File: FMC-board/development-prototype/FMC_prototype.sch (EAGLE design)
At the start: 83 parts, among them J1 PJ-102AH, J2 DC_POWER_JACK-PJ-102AH, U1 TPS79301, U10 ADN4664, U11 ADN4663, U2 TPS79333, U3 ADN4663, U4 ADN4663, U5 ADN4664, U6 PDS1-S12-S5-S, U7 TPS79301, U9 ADN4664

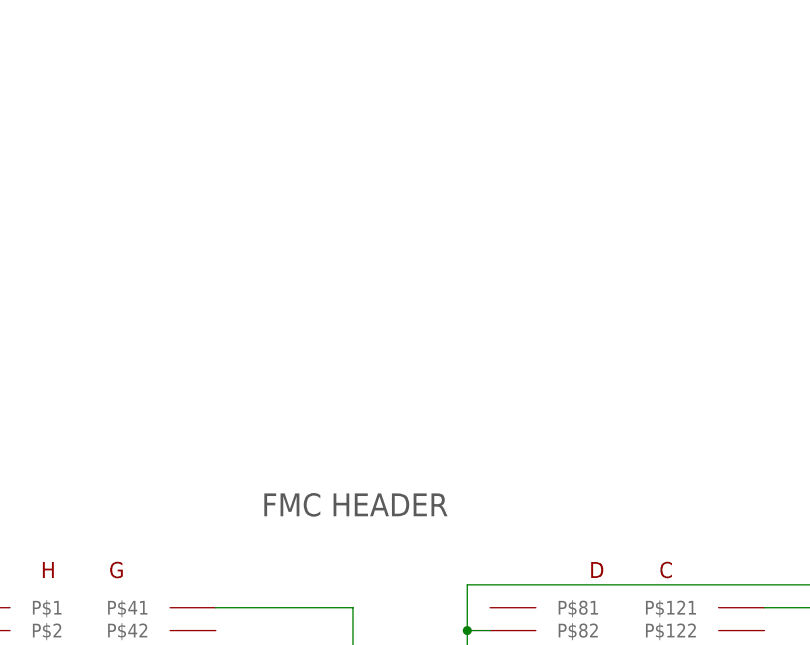
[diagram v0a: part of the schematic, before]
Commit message: Toward meeting fmc standards
- I read the VITA 57.1 standard and I think it would be worth it to make
  the board marginally compliant (even on first run) because it is not
  very dense and this really will inform the future design of the board
- Also, it will make it compatible with 100's of carrier boards with all
  sorts of FPGAs and DSPs onboard
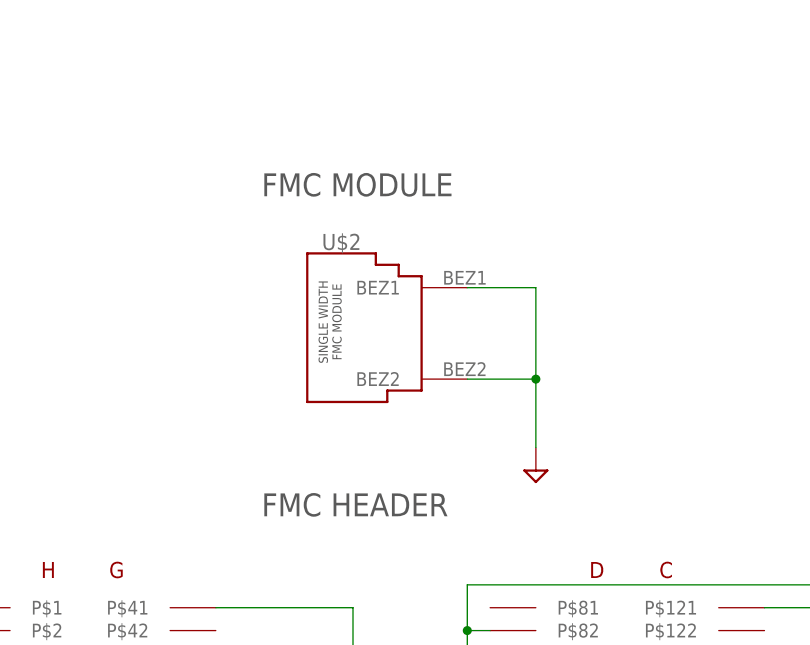
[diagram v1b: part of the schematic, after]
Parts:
- added U$2: FMC_SINGLE_WIDTH_MODULE, jonnew:FMC_SINGLE_WIDTH_MODULE
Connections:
- net GND_ISO: now also U$2.BEZ1, U$2.BEZ2
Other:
- note added: "FMC MODULE"
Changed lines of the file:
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@@
 <part name="GND15" library="supply1" deviceset="GND" device=""/>
 <part name="PWR1" library="jonnew" deviceset="+3V3" device=""/>
+<part name="U$2" library="jonnew" deviceset="FMC_SINGLE_WIDTH_MODULE" device=""/>
+<part name="PWR2" library="jonnew" deviceset="GND_ISO" device=""/>
 </parts>
 <sheets>
@@
 <text x="233.68" y="20.32" size="2.54" layer="97" rot="R90">AQ. BOARD SIDE</text>
 <text x="424.18" y="314.96" size="2.54" layer="97">FMC HEADER</text>
+<text x="424.18" y="350.52" size="2.54" layer="97">FMC MODULE</text>
 </plain>
 <instances>
@@
 <instance part="GND15" gate="1" x="434.34" y="200.66" rot="MR0"/>
 <instance part="PWR1" gate="PWR1" x="459.74" y="198.12"/>
+<instance part="U$2" gate="G$1" x="441.96" y="335.28"/>
+<instance part="PWR2" gate="G$1" x="454.66" y="322.58"/>
 </instances>
 <busses>
@@
 <junction x="91.44" y="96.52"/>
 <pinref part="GND64" gate="G$1" pin="GND_ISO"/>
+</segment>
+<segment>
+<pinref part="U$2" gate="G$1" pin="BEZ2"/>
+<wire x1="447.04" y1="330.2" x2="454.66" y2="330.2" width="0.1524" layer="91"/>
+<wire x1="454.66" y1="330.2" x2="454.66" y2="322.58" width="0.1524" layer="91"/>
+<pinref part="U$2" gate="G$1" pin="BEZ1"/>
+<wire x1="447.04" y1="340.36" x2="454.66" y2="340.36" width="0.1524" layer="91"/>
+<wire x1="454.66" y1="340.36" x2="454.66" y2="330.2" width="0.1524" layer="91"/>
+<junction x="454.66" y="330.2"/>
+<pinref part="PWR2" gate="G$1" pin="GND_ISO"/>
 </segment>
 </net>
@@
 </schematic>
 </drawing>
+<compatibility>
+<note version="6.3" minversion="6.2.2" severity="warning">
+Since Version 6.2.2 text objects can contain more than one line,
+which will not be processed correctly with this version.
+</note>
+</compatibility>
 </eagle>

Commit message: Toward VITA-57.1 compliance
- Found pad alignment issues in the SOIC16 digital isolation chips.
  Fixed that.
- Layout changes informed by VITA 57.1 and several FMC modules designed
  by CERN for data collection in high-energy physics experiments.
- Removed power jacks for now. Replaced with simple headers and reverse
  polarity protection to make up for the automatic polarity protection
  given by center positive jack (assuming the user uses the correct wall
  wart).
- High-frequency layout improvments
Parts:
- removed J1: PJ-102AH, RHD2000_eval_board:DC_POWER_JACK-PJ-102AH
- removed J2: DC_POWER_JACK-PJ-102AH, RHD2000_eval_board:DC_POWER_JACK-PJ-102AH
- removed TP1, TP2, TP3, TP4, TP5: TP5P5-25-13, testpad:TP5P5-25-13
- added C17, C20, C24, C27, C28, C29: 100n, RHD2000_eval_board:C_0603
- added C30, C31: 22uF, jonnew:C-POL_1210
- added D4: 8V, jonnew:Z-DIODE_SOD-323
- added R13: 10k, RHD2000_eval_board:R_0603
- added U$3: (no value), jonnew:JP2E_THRU-HOLE
- added U$4: SSM3J328R, jonnew:P-MOSFET_SOT23-GSD
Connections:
- removed net VDD_IN: C16.1, J2.PWR, LINK-5V.1, TP4D.TP, U7.EN, U7.IN
- new net AUX_VDD: C16.1, D4.C, LINK-5V.1, U$4.S, U7.EN, U7.IN
- new net N$6: D4.A, R13.2, U$4.G
- new net N$7: U$3.1, U$4.D
- net +3V3: now also C17.2, C20.2, C24.2, C27.2; no longer TP4B.TP, TP4C.TP
- net +3V3_ISO: no longer TP3C.TP
- net +3V6: no longer TP4A.TP
- net +3V6_ISO: no longer TP3B.TP
- net +5V0_EXT: no longer J1.PWR
- net +5V0_ISO: no longer TP3D.TP
- net 12V_FPGA: now also C28.2, C29.2, C30.+, C31.+
- net B_CS+: no longer TP5A.TP
- net B_MISO1+: no longer TP5D.TP
- net B_MISO2+: no longer TP5E.TP
- net B_MOSI+: no longer TP5C.TP
- net B_SCLK+: no longer TP5B.TP
- net GND: now also C17.1, C20.1, C24.1, C27.1, C28.1, C29.1, C30.-, C31.-, R13.1, U$3.2; no longer J2.GND1, J2.GND2, TP2E.TP, TP4E.TP
- net GND_ISO: no longer J1.GND1, J1.GND2, TP1A.TP, TP3A.TP, TP3E.TP
- net MISO1+: no longer TP2B.TP
- net MISO1+_ISOLATED: no longer TP1D.TP
- net MISO1_ISOLATED_SE: no longer TP1E.TP
- net MISO1_SE: no longer TP2A.TP
- net MOSI+: no longer TP2D.TP
- net MOSI+_ISOLATED: no longer TP1B.TP
- net MOSI_ISOLATED_SE: no longer TP1C.TP
- net MOSI_SE: no longer TP2C.TP
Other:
- moved on the sheet: C10_DIR, C11_DIR, C14_DIR, C15_DIR, C18_DIR

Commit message: About 50% through routing
- The FMC<->Driver/Reciver<->Isolator<->Driver/Receiver path needs to be
  rearranged to minimize crossovers
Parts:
- removed D1, D2: SML-D1, jonnew:LED_0603
- added C32, C34, C35, C37: 10uF, jonnew:C-POL_1206
- added VDD_AUX: (no value), jonnew:JP2E_THRU-HOLE
- U$3: device jonnew:JP2E_THRU-HOLE -> jonnew:LED_2X_VERTICAL
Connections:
- net +3V3: now also C35.+, C37.+
- net +3V3_ISO: now also C32.+, C34.+
- net GND: now also C35.-, C37.-, VDD_AUX.2; no longer U$3.2
- net GND_ISO: now also C32.-, C34.-, U$31.C, U$32.C; no longer D1.C, D2.C
- net N$10: now also U$31.A; no longer D2.A
- net N$11: now also U$32.A; no longer D1.A
- net N$7: now also VDD_AUX.1; no longer U$3.1
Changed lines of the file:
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@@
 <part name="R12" library="RHD2000_eval_board" deviceset="R" device="_0603" value="820"/>
 <part name="PWR22" library="jonnew" deviceset="+3V6" device=""/>
-<part name="D2" library="jonnew" deviceset="LED" device="_0603" value="SML-D1"/>
 <part name="R2" library="RHD2000_eval_board" deviceset="R" device="_0603" value="820"/>
-<part name="D1" library="jonnew" deviceset="LED" device="_0603" value="SML-D1"/>
 <part name="R1" library="RHD2000_eval_board" deviceset="R" device="_0603" value="820"/>
 <part name="C10_DIR" library="jonnew" deviceset="COAX" device="_SMA-VERT" value="142-0701"/>
@@
 <part name="U$2" library="jonnew" deviceset="FMC_SINGLE_WIDTH_MODULE" device=""/>
 <part name="PWR2" library="jonnew" deviceset="GND_ISO" device=""/>
-<part name="U$3" library="jonnew" deviceset="JP2E" device="_THRU-HOLE"/>
+<part name="VDD_AUX" library="jonnew" deviceset="JP2E" device="_THRU-HOLE"/>
 <part name="D4" library="jonnew" deviceset="Z-DIODE" device="_SOD-323" value="8V"/>
 <part name="U$4" library="jonnew" deviceset="P-MOSFET" device="_SOT23-GSD" value="SSM3J328R"/>
@@
 <part name="GND30" library="supply1" deviceset="GND" device=""/>
 <part name="GND31" library="supply1" deviceset="GND" device=""/>
+<part name="C32" library="jonnew" deviceset="C-POL" device="_1206" value="10uF"/>
+<part name="GND33" library="jonnew" deviceset="GND_ISO" device=""/>
+<part name="C34" library="jonnew" deviceset="C-POL" device="_1206" value="10uF"/>
+<part name="GND34" library="jonnew" deviceset="GND_ISO" device=""/>
+<part name="C35" library="jonnew" deviceset="C-POL" device="_1206" value="10uF"/>
+<part name="C37" library="jonnew" deviceset="C-POL" device="_1206" value="10uF"/>
+<part name="GND35" library="supply1" deviceset="GND" device=""/>
+<part name="GND37" library="supply1" deviceset="GND" device=""/>
+<part name="U$3" library="jonnew" deviceset="LED_2X" device="_VERTICAL"/>
 </parts>
 <sheets>
@@
 <instance part="R12" gate="R" x="332.74" y="332.74" rot="R270"/>
 <instance part="PWR22" gate="PWR#" x="340.36" y="342.9"/>
-<instance part="D2" gate="G$1" x="106.68" y="271.78"/>
 <instance part="R2" gate="R" x="106.68" y="281.94" rot="R270"/>
-<instance part="D1" gate="G$1" x="106.68" y="322.58"/>
 <instance part="R1" gate="R" x="106.68" y="332.74" rot="R270"/>
 <instance part="C10_DIR" gate="G$1" x="533.4" y="266.7" rot="MR0"/>
@@
 <instance part="U$2" gate="G$1" x="441.96" y="335.28"/>
 <instance part="PWR2" gate="G$1" x="454.66" y="322.58"/>
-<instance part="U$3" gate="G$1" x="332.74" y="386.08" rot="R270"/>
+<instance part="VDD_AUX" gate="G$1" x="332.74" y="386.08" rot="R270"/>
 <instance part="D4" gate="G$1" x="299.72" y="381" rot="R90"/>
 <instance part="U$4" gate="G$1" x="312.42" y="386.08" rot="R90"/>
@@
 <instance part="GND30" gate="1" x="454.66" y="142.24" rot="MR0"/>
 <instance part="GND31" gate="1" x="444.5" y="142.24" rot="MR0"/>
+<instance part="C32" gate="C" x="144.78" y="210.82" rot="R270"/>
+<instance part="GND33" gate="G$1" x="137.16" y="208.28"/>
+<instance part="C34" gate="C" x="144.78" y="121.92" rot="R270"/>
+<instance part="GND34" gate="G$1" x="139.7" y="119.38"/>
+<instance part="C35" gate="C" x="276.86" y="208.28" rot="R270"/>
+<instance part="C37" gate="C" x="276.86" y="121.92" rot="R270"/>
+<instance part="GND35" gate="1" x="271.78" y="116.84"/>
+<instance part="GND37" gate="1" x="271.78" y="203.2"/>
+<instance part="U$3" gate="1" x="106.68" y="271.78"/>
+<instance part="U$3" gate="2" x="106.68" y="322.58"/>
 </instances>
 <busses>
@@
 <wire x1="134.62" y1="261.62" x2="134.62" y2="274.32" width="0.1524" layer="91"/>
 <pinref part="GND56" gate="G$1" pin="GND_ISO"/>
-<pinref part="D2" gate="G$1" pin="C"/>
 <wire x1="106.68" y1="266.7" x2="106.68" y2="261.62" width="0.1524" layer="91"/>
 <wire x1="134.62" y1="261.62" x2="106.68" y2="261.62" width="0.1524" layer="91"/>
 <junction x="134.62" y="261.62"/>
+<pinref part="U$3" gate="1" pin="C"/>
 </segment>
 <segment>
@@
 <wire x1="182.88" y1="325.12" x2="182.88" y2="309.88" width="0.1524" layer="91"/>
 <pinref part="GND55" gate="G$1" pin="GND_ISO"/>
-<pinref part="D1" gate="G$1" pin="C"/>
 <wire x1="106.68" y1="317.5" x2="106.68" y2="309.88" width="0.1524" layer="91"/>
 <wire x1="116.84" y1="309.88" x2="106.68" y2="309.88" width="0.1524" layer="91"/>
 <junction x="116.84" y="309.88"/>
+<pinref part="U$3" gate="2" pin="C"/>
 </segment>
 <segment>
@@
 <junction x="454.66" y="330.2"/>
 <pinref part="PWR2" gate="G$1" pin="GND_ISO"/>
+</segment>
+<segment>
+<pinref part="C32" gate="C" pin="-"/>
+<wire x1="142.24" y1="210.82" x2="137.16" y2="210.82" width="0.1524" layer="91"/>
+<wire x1="137.16" y1="210.82" x2="137.16" y2="208.28" width="0.1524" layer="91"/>
+<pinref part="GND33" gate="G$1" pin="GND_ISO"/>
+</segment>
+<segment>
+<pinref part="C34" gate="C" pin="-"/>
+<wire x1="142.24" y1="121.92" x2="139.7" y2="121.92" width="0.1524" layer="91"/>
+<wire x1="139.7" y1="121.92" x2="139.7" y2="119.38" width="0.1524" layer="91"/>
+<pinref part="GND34" gate="G$1" pin="GND_ISO"/>
 </segment>
 </net>
@@
 </segment>
 <segment>
-<pinref part="U$3" gate="G$1" pin="2"/>
+<pinref part="VDD_AUX" gate="G$1" pin="2"/>
 <wire x1="332.74" y1="383.54" x2="330.2" y2="383.54" width="0.1524" layer="91"/>
 <pinref part="GND10" gate="1" pin="GND"/>
@@
 <pinref part="GND16" gate="1" pin="GND"/>
 <wire x1="444.5" y1="172.72" x2="444.5" y2="170.18" width="0.1524" layer="91"/>
+</segment>
+<segment>
+<pinref part="C37" gate="C" pin="-"/>
+<wire x1="274.32" y1="121.92" x2="271.78" y2="121.92" width="0.1524" layer="91"/>
+<wire x1="271.78" y1="121.92" x2="271.78" y2="119.38" width="0.1524" layer="91"/>
+<pinref part="GND35" gate="1" pin="GND"/>
+</segment>
+<segment>
+<pinref part="C35" gate="C" pin="-"/>
+<wire x1="274.32" y1="208.28" x2="271.78" y2="208.28" width="0.1524" layer="91"/>
+<wire x1="271.78" y1="208.28" x2="271.78" y2="205.74" width="0.1524" layer="91"/>
+<pinref part="GND37" gate="1" pin="GND"/>
 </segment>
 </net>
@@
 <wire x1="292.1" y1="121.92" x2="299.72" y2="121.92" width="0.1524" layer="91"/>
 <junction x="292.1" y="121.92"/>
+<pinref part="C37" gate="C" pin="+"/>
+<wire x1="281.94" y1="121.92" x2="292.1" y2="121.92" width="0.1524" layer="91"/>
 </segment>
 <segment>
@@
 <wire x1="289.56" y1="208.28" x2="297.18" y2="208.28" width="0.1524" layer="91"/>
 <junction x="289.56" y="208.28"/>
+<pinref part="C35" gate="C" pin="+"/>
+<wire x1="281.94" y1="208.28" x2="289.56" y2="208.28" width="0.1524" layer="91"/>
 </segment>
 <segment>
@@
 <wire x1="162.56" y1="121.92" x2="167.64" y2="121.92" width="0.1524" layer="91"/>
 <label x="154.94" y="121.92" size="1.778" layer="95"/>
+<pinref part="C34" gate="C" pin="+"/>
+<wire x1="149.86" y1="121.92" x2="162.56" y2="121.92" width="0.1524" layer="91"/>
+<junction x="162.56" y="121.92"/>
 </segment>
 <segment>
@@
 <wire x1="160.02" y1="205.74" x2="160.02" y2="210.82" width="0.1524" layer="91"/>
 <label x="152.4" y="210.82" size="1.778" layer="95"/>
+<pinref part="C32" gate="C" pin="+"/>
+<wire x1="149.86" y1="210.82" x2="160.02" y2="210.82" width="0.1524" layer="91"/>
+<junction x="160.02" y="210.82"/>
 </segment>
 <segment>
@@
 <segment>
 <pinref part="R2" gate="R" pin="2"/>
-<pinref part="D2" gate="G$1" pin="A"/>
 <wire x1="106.68" y1="276.86" x2="106.68" y2="274.32" width="0.1524" layer="91"/>
+<pinref part="U$3" gate="1" pin="A"/>
 </segment>
 </net>
@@
 <segment>
 <pinref part="R1" gate="R" pin="2"/>
-<pinref part="D1" gate="G$1" pin="A"/>
 <wire x1="106.68" y1="327.66" x2="106.68" y2="325.12" width="0.1524" layer="91"/>
+<pinref part="U$3" gate="2" pin="A"/>
 </segment>
 </net>
@@
 <pinref part="U$4" gate="G$1" pin="D"/>
 <wire x1="317.5" y1="386.08" x2="332.74" y2="386.08" width="0.1524" layer="91"/>
-<pinref part="U$3" gate="G$1" pin="1"/>
-</segment>
-</net>
+<pinref part="VDD_AUX" gate="G$1" pin="1"/>
+</segment>
+</net>

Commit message: Removed FPGA side LVDS drivers/receivers
- Not needed as all FMC connections can be configured as single
  ended
- Started BOM
- Switched to RA SMAs on the panel side of board
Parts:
- removed C10_DIR, C11_DIR, C14_DIR, C15_DIR, C18_DIR: 142-0701, jonnew:COAX_SMA-VERT
- removed C21, C22, C23: 100n, RHD2000_eval_board:C_0603
- removed C35, C37: 10uF, jonnew:C-POL_1206
- removed R10, R11: 10k, RHD2000_eval_board:R_0603
- removed R14, R15, R16, R17, R18, R19, R20, R21, R22, R23: 0, RHD2000_eval_board:R_0603
- removed U10, U9: ADN4664, jonnew:ADN4664_SOIC
- removed U11: ADN4663, jonnew:ADN4663_SOIC
- added TP_C10, TP_C11, TP_C14, TP_C15, TP_C18: 142-0701, jonnew:COAX_SMA-VERT
- G22_ISO, H21_ISO, H22_ISO: device jonnew:COAX_SMA-VERT -> jonnew:COAX_CONREVSMA002-G
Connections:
- net MISO1_ISOLATED_SE renamed MISO1_ISO
- net MISO2_ISOLATED_SE renamed MISO2_ISO
- net TP1_FROM_SMA renamed TP_G7N_ISO
- net TP2_FROM_SMA renamed TP_G6P_ISO
- net TP3_FROM_FPGA renamed G22
- removed net CS+: FMCG$1.P$19, R15.2, U10.RIN1+
- removed net CS-: FMCG$1.P$20, R14.2, U10.RIN1-
- removed net CS_SE: DO_ISO.VIB, U10.ROUT1
- removed net MISO1+: FMCG$1.P$10, R21.2, U11.DOUT2+
- removed net MISO1-: FMCG$1.P$11, R20.2, U11.DOUT2-
- removed net MISO1_SE: DI_ISO.VOB, U11.DIN2
- removed net MISO2+: FMCG$1.P$7, R23.2, U11.DOUT1+
- removed net MISO2-: FMCG$1.P$8, R22.2, U11.DOUT1-
- removed net MISO2_SE: DI_ISO.VOA, U11.DIN1
- removed net MOSI+: FMCG$1.P$13, R19.2, U9.RIN2+
- removed net MOSI-: FMCG$1.P$14, R18.2, U9.RIN2-
- removed net MOSI_SE: DO_ISO.VID, U9.ROUT2
- removed net N$3: R10.2, U10.RIN2-
- removed net SCLK+: FMCG$1.P$16, R17.2, U9.RIN1+
- removed net SCLK-: FMCG$1.P$17, R16.2, U9.RIN1-
- removed net SCLK_SE: DO_ISO.VIC, U9.ROUT1
- removed net TP1_TO_FPGA: DI_ISO.VOC, FMCG$1.P$22
- removed net TP2_TO_FPGA: DI_ISO.VOD, FMCG$1.P$23
- removed net TP4: C10_DIR.1, FMCG$1.P$130
- removed net TP5: C11_DIR.1, FMCG$1.P$131
- removed net TP6: C14_DIR.1, FMCG$1.P$134
- removed net TP8: C18_DIR.1, FMCG$1.P$138
- new net C10: FMCG$1.P$130
- new net C11: FMCG$1.P$131
- new net C14: FMCG$1.P$134
- new net C18: FMCG$1.P$138
- new net CS: DO_ISO.VIB
- new net G6: DI_ISO.VOD, FMCG$1.P$46
- new net G7: DI_ISO.VOC, FMCG$1.P$47
- new net MISO1: DI_ISO.VOA, FMCG$1.P$8
- new net MISO2: DI_ISO.VOB, FMCG$1.P$7
- new net MOSI: DO_ISO.VID, FMCG$1.P$10
- new net SCLK: DO_ISO.VIC, FMCG$1.P$11
- net +3V3: now also FMCG$1.P$76; no longer C21.1, C22.1, C23.1, C35.+, C37.+, U10.VCC, U11.VCC, U9.VCC
- net A_CS+: no longer R15.1
- net A_CS-: no longer R14.1
- net A_MISO1+: no longer R21.1
- net A_MISO1-: no longer R20.1
- net A_MISO2+: no longer R23.1
- net A_MISO2-: no longer R22.1
- net A_MOSI+: no longer R19.1
- net A_MOSI-: no longer R18.1
- net A_SCLK+: no longer R17.1
- net A_SCLK-: no longer R16.1
- net GND: now also TP_C10.2, TP_C11.2, TP_C14.2, TP_C15.2; no longer C10_DIR.2, C11_DIR.2, C14_DIR.2, C15_DIR.2, C18_DIR.2, C21.2, C22.2, C23.2, C35.-, C37.-, FMCG$1.P$102, FMCG$1.P$105, FMCG$1.P$108, FMCG$1.P$117, FMCG$1.P$119, FMCG$1.P$82, FMCG$1.P$83, FMCG$1.P$86, FMCG$1.P$87, FMCG$1.P$90, FMCG$1.P$93, FMCG$1.P$96, FMCG$1.P$99, R10.1, R11.1, U10.GND, U11.GND, U9.GND
- net N$1: now also FMCG$1.P$102, FMCG$1.P$105, FMCG$1.P$108, FMCG$1.P$117, FMCG$1.P$119, FMCG$1.P$82, FMCG$1.P$83, FMCG$1.P$86, FMCG$1.P$87, FMCG$1.P$90, FMCG$1.P$93, FMCG$1.P$96, FMCG$1.P$99; no longer R11.2, U10.RIN2+
- net TP7: no longer C15_DIR.1

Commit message: Lots of routing simplification
- Moved non-isolated SPI buses onto there own IO on the FMC connector
  since there is plenty of that. Got rid of the branches and jumper
  resistors as a result.
- Only a bit more wiring todo before be ERC/DRC stage.
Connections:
- removed net CS_ISOLATED_SE: DO_ISO.VOB, U4.DIN1
- removed net G22: DO_ISO.VIA, FMCG$1.P$62
- removed net G6: DI_ISO.VOD, FMCG$1.P$46
- removed net G7: DI_ISO.VOC, FMCG$1.P$47
- removed net MOSI_ISOLATED_SE: DO_ISO.VOD, U3.DIN2
- removed net N$1: FMCG$1.P$102, FMCG$1.P$105, FMCG$1.P$108, FMCG$1.P$117, FMCG$1.P$119, FMCG$1.P$82, FMCG$1.P$83, FMCG$1.P$86, FMCG$1.P$87, FMCG$1.P$90, FMCG$1.P$93, FMCG$1.P$96, FMCG$1.P$99
- removed net SCLK_ISOLATED_SE: DO_ISO.VOC, U3.DIN1
- removed net TP3_TO_SMA: DO_ISO.VOA, G22_ISO.1
- removed net TP_G6P_ISO: DI_ISO.VID, H22_ISO.1
- removed net TP_G7N_ISO: DI_ISO.VIC, H21_ISO.1
- new net CS_ISO: DO_ISO.VOA, U4.DIN1
- new net H17: DO_ISO.VID, FMCG$1.P$17
- new net H22: DI_ISO.VOB, FMCG$1.P$22
- new net H23: DI_ISO.VOA, FMCG$1.P$23
- new net MOSI_ISO: DO_ISO.VOC, U3.DIN2
- new net N$9: FMCG$1.P$76
- new net SCLK_ISO: DO_ISO.VOB, U3.DIN1
- net +3V3: no longer FMCG$1.P$76
- net A_CS+: now also FMCG$1.P$58
- net A_CS-: now also FMCG$1.P$59
- net A_MISO1+: now also FMCG$1.P$49
- net A_MISO1-: now also FMCG$1.P$50
- net A_MISO2+: now also FMCG$1.P$46
- net A_MISO2-: now also FMCG$1.P$47
- net A_MOSI+: now also FMCG$1.P$52
- net A_MOSI-: now also FMCG$1.P$53
- net A_SCLK+: now also FMCG$1.P$55
- net A_SCLK-: now also FMCG$1.P$56
- net CS: now also DO_ISO.VIA, FMCG$1.P$13; no longer DO_ISO.VIB
- net GND: now also FMCG$1.P$102, FMCG$1.P$105, FMCG$1.P$108, FMCG$1.P$117, FMCG$1.P$119, FMCG$1.P$82, FMCG$1.P$83, FMCG$1.P$86, FMCG$1.P$87, FMCG$1.P$90, FMCG$1.P$93, FMCG$1.P$96, FMCG$1.P$99
- net MISO1: now also DI_ISO.VOD, FMCG$1.P$19; no longer DI_ISO.VOA, FMCG$1.P$8
- net MISO2: now also DI_ISO.VOC, FMCG$1.P$20; no longer DI_ISO.VOB, FMCG$1.P$7
- net MOSI: now also DO_ISO.VIC, FMCG$1.P$16; no longer DO_ISO.VID, FMCG$1.P$10
- net SCLK: now also DO_ISO.VIB, FMCG$1.P$14; no longer DO_ISO.VIC, FMCG$1.P$11
